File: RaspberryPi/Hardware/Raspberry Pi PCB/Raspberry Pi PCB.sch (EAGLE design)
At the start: 32 parts, among them Q11 BSS138, Q12 BSS138, Q2 BSS138

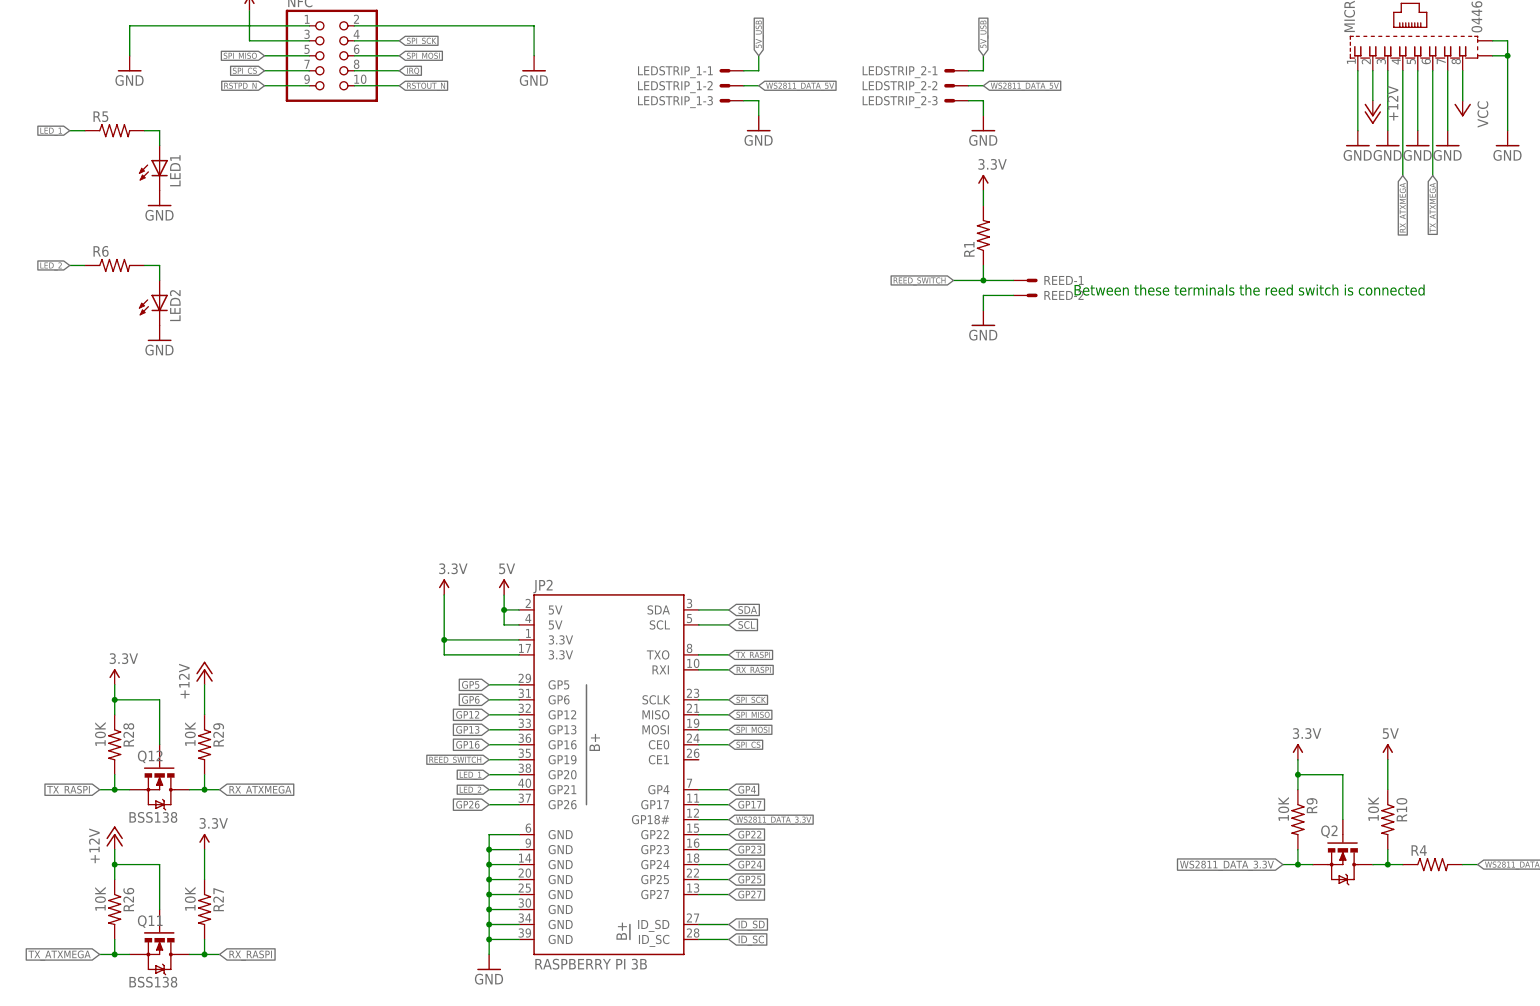
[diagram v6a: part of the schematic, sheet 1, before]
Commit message: Finished the first version of the Raspberry PCB.
Design rule check worked out fine. The PCB should now be ready for ordering.
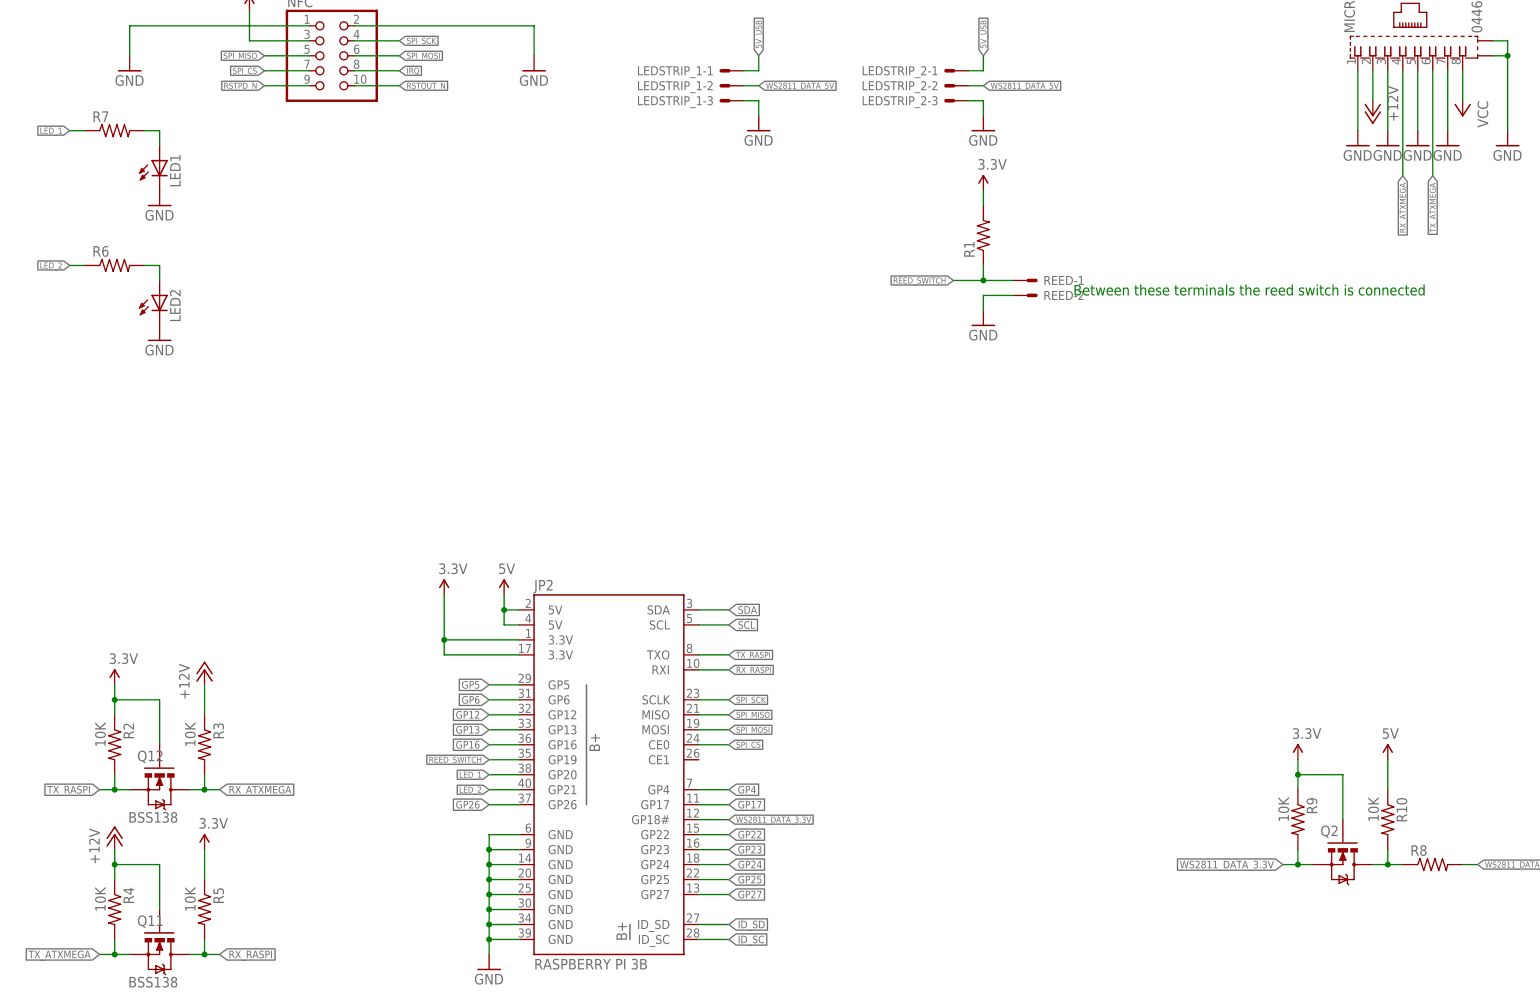
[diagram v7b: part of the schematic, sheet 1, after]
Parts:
- removed R26, R27: 10K, SparkFun:RESISTOR0603-RES
- added R7, R8: (no value), adafruit:R-US_R0805
- R4, R5: value (none) -> 10K; device adafruit:R-US_R0805 -> SparkFun:RESISTOR0603-RES
- renumbered C11 to C8, R28 to R2, R29 to R3
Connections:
- net +12V: now also R4.1; no longer R26.1
- net 3.3V: now also R5.1; no longer R27.1
- net LED_1: now also R7.1; no longer R5.1
- net N$3: now also R8.1; no longer R4.1
- net N$5: now also R7.2; no longer R5.2
- net RX_RASPI: now also R5.2; no longer R27.2
- net TX_ATXMEGA: now also R4.2; no longer R26.2
- net WS2811_DATA_5V: now also R8.2; no longer R4.2
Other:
- moved on the sheet: R4, R5
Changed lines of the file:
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@@
 <part name="SUPPLY14" library="SparkFun-Aesthetics" deviceset="3.3V" device=""/>
 <part name="Q11" library="SparkFun" deviceset="MOSFET-NCHANNEL" device="SMD" value="BSS138"/>
-<part name="R26" library="SparkFun" deviceset="RESISTOR" device="0603-RES" value="10K"/>
-<part name="R27" library="SparkFun" deviceset="RESISTOR" device="0603-RES" value="10K"/>
+<part name="R4" library="SparkFun" deviceset="RESISTOR" device="0603-RES" value="10K"/>
+<part name="R5" library="SparkFun" deviceset="RESISTOR" device="0603-RES" value="10K"/>
 <part name="Q12" library="SparkFun" deviceset="MOSFET-NCHANNEL" device="SMD" value="BSS138"/>
-<part name="R28" library="SparkFun" deviceset="RESISTOR" device="0603-RES" value="10K"/>
-<part name="R29" library="SparkFun" deviceset="RESISTOR" device="0603-RES" value="10K"/>
+<part name="R2" library="SparkFun" deviceset="RESISTOR" device="0603-RES" value="10K"/>
+<part name="R3" library="SparkFun" deviceset="RESISTOR" device="0603-RES" value="10K"/>
 <part name="P+51" library="supply1" library_urn="urn:adsk.eagle:library:371" deviceset="+12V" device=""/>
 <part name="P+52" library="supply1" library_urn="urn:adsk.eagle:library:371" deviceset="+12V" device=""/>
@@
 <part name="GND21" library="SparkFun" deviceset="GND" device=""/>
 <part name="GND22" library="SparkFun" deviceset="GND" device=""/>
-<part name="R4" library="adafruit" library_urn="urn:adsk.eagle:library:420" deviceset="R-US_" device="R0805"/>
-<part name="R5" library="adafruit" deviceset="R-US_" device="R0805"/>
+<part name="R8" library="adafruit" library_urn="urn:adsk.eagle:library:420" deviceset="R-US_" device="R0805"/>
+<part name="R7" library="adafruit" deviceset="R-US_" device="R0805"/>
 <part name="R6" library="adafruit" deviceset="R-US_" device="R0805"/>
 <part name="GND23" library="SparkFun" deviceset="GND" device=""/>
@@
 <part name="SUPPLY9" library="SparkFun-Aesthetics" deviceset="5V" device=""/>
 <part name="SUPPLY8" library="SparkFun-Aesthetics" deviceset="5V" device=""/>
-<part name="C11" library="SparkFun-Capacitors" library_urn="urn:adsk.eagle:library:510" deviceset="1.0UF" device="-0805-25V-(+80/-20%)" package3d_urn="urn:adsk.eagle:package:37429/1" value="100nF"/>
+<part name="C8" library="SparkFun-Capacitors" library_urn="urn:adsk.eagle:library:510" deviceset="1.0UF" device="-0805-25V-(+80/-20%)" package3d_urn="urn:adsk.eagle:package:37429/1" value="100nF"/>
 <part name="GND25" library="supply1" library_urn="urn:adsk.eagle:library:371" deviceset="GND" device=""/>
 <part name="USB_POWER" library="87520-0010BLF" deviceset="87520-0010BLF" device=""/>
@@
 <attribute name="VALUE" x="22.606" y="4.572" size="1.778" layer="96"/>
 </instance>
-<instance part="R26" gate="G$1" x="20.32" y="17.78" rot="R270"/>
-<instance part="R27" gate="G$1" x="35.56" y="17.78" rot="R270"/>
+<instance part="R4" gate="G$1" x="20.32" y="17.78" rot="R270"/>
+<instance part="R5" gate="G$1" x="35.56" y="17.78" rot="R270"/>
 <instance part="Q12" gate="G$1" x="27.94" y="38.1" smashed="yes" rot="R270">
 <attribute name="NAME" x="24.13" y="42.926" size="1.778" layer="95"/>
 <attribute name="VALUE" x="22.606" y="32.512" size="1.778" layer="96"/>
 </instance>
-<instance part="R28" gate="G$1" x="20.32" y="45.72" rot="R270"/>
-<instance part="R29" gate="G$1" x="35.56" y="45.72" rot="R270"/>
+<instance part="R2" gate="G$1" x="20.32" y="45.72" rot="R270"/>
+<instance part="R3" gate="G$1" x="35.56" y="45.72" rot="R270"/>
 <instance part="P+51" gate="1" x="35.56" y="58.42"/>
 <instance part="P+52" gate="1" x="20.32" y="30.48"/>
@@
 <instance part="GND21" gate="1" x="167.64" y="149.86"/>
 <instance part="GND22" gate="1" x="129.54" y="149.86"/>
-<instance part="R4" gate="G$1" x="243.84" y="25.4"/>
-<instance part="R5" gate="G$1" x="20.32" y="149.86"/>
+<instance part="R8" gate="G$1" x="243.84" y="25.4"/>
+<instance part="R7" gate="G$1" x="20.32" y="149.86"/>
 <instance part="R6" gate="G$1" x="20.32" y="127"/>
 <instance part="GND23" gate="1" x="27.94" y="137.16"/>
@@
 <wire x1="27.94" y1="53.34" x2="20.32" y2="53.34" width="0.1524" layer="91"/>
 <junction x="20.32" y="53.34"/>
-<pinref part="R28" gate="G$1" pin="1"/>
+<pinref part="R2" gate="G$1" pin="1"/>
 <pinref part="Q12" gate="G$1" pin="G"/>
 <pinref part="SUPPLY1" gate="G$1" pin="3.3V"/>
@@
 <segment>
 <wire x1="35.56" y1="22.86" x2="35.56" y2="27.94" width="0.1524" layer="91"/>
-<pinref part="R27" gate="G$1" pin="1"/>
+<pinref part="R5" gate="G$1" pin="1"/>
 <pinref part="SUPPLY2" gate="G$1" pin="3.3V"/>
 </segment>
@@
 </segment>
 <segment>
-<pinref part="R5" gate="G$1" pin="1"/>
+<pinref part="R7" gate="G$1" pin="1"/>
 <wire x1="15.24" y1="149.86" x2="12.7" y2="149.86" width="0.1524" layer="91"/>
 <label x="12.7" y="149.86" size="1.016" layer="95" rot="R180" xref="yes"/>
@@
 <junction x="20.32" y="38.1"/>
 <pinref part="Q12" gate="G$1" pin="S"/>
-<pinref part="R28" gate="G$1" pin="2"/>
+<pinref part="R2" gate="G$1" pin="2"/>
 <label x="17.78" y="38.1" size="1.27" layer="95" rot="R180" xref="yes"/>
 </segment>
@@
 <segment>
 <wire x1="35.56" y1="50.8" x2="35.56" y2="55.88" width="0.1524" layer="91"/>
-<pinref part="R29" gate="G$1" pin="1"/>
+<pinref part="R3" gate="G$1" pin="1"/>
 <pinref part="P+51" gate="1" pin="+12V"/>
 </segment>
@@
 <wire x1="27.94" y1="25.4" x2="20.32" y2="25.4" width="0.1524" layer="91"/>
 <junction x="20.32" y="25.4"/>
-<pinref part="R26" gate="G$1" pin="1"/>
+<pinref part="R4" gate="G$1" pin="1"/>
 <pinref part="Q11" gate="G$1" pin="G"/>
 <pinref part="P+52" gate="1" pin="+12V"/>
@@
 <junction x="35.56" y="38.1"/>
 <pinref part="Q12" gate="G$1" pin="D"/>
-<pinref part="R29" gate="G$1" pin="2"/>
+<pinref part="R3" gate="G$1" pin="2"/>
 <label x="38.1" y="38.1" size="1.27" layer="95" xref="yes"/>
 </segment>
@@
 <junction x="20.32" y="10.16"/>
 <pinref part="Q11" gate="G$1" pin="S"/>
-<pinref part="R26" gate="G$1" pin="2"/>
+<pinref part="R4" gate="G$1" pin="2"/>
 <label x="17.78" y="10.16" size="1.27" layer="95" rot="R180" xref="yes"/>
 </segment>
@@
 <junction x="35.56" y="10.16"/>
 <pinref part="Q11" gate="G$1" pin="D"/>
-<pinref part="R27" gate="G$1" pin="2"/>
+<pinref part="R5" gate="G$1" pin="2"/>
 <label x="38.1" y="10.16" size="1.27" layer="95" xref="yes"/>
 </segment>
@@
 <segment>
 <pinref part="LED1" gate="G$1" pin="A"/>
-<pinref part="R5" gate="G$1" pin="2"/>
+<pinref part="R7" gate="G$1" pin="2"/>
 <wire x1="27.94" y1="147.32" x2="27.94" y2="149.86" width="0.1524" layer="91"/>
 <wire x1="27.94" y1="149.86" x2="25.4" y2="149.86" width="0.1524" layer="91"/>
@@
 </segment>
 <segment>
-<pinref part="R4" gate="G$1" pin="2"/>
+<pinref part="R8" gate="G$1" pin="2"/>
 <wire x1="248.92" y1="25.4" x2="251.46" y2="25.4" width="0.1524" layer="91"/>
 <label x="251.46" y="25.4" size="1.016" layer="95" xref="yes"/>
@@
 <net name="N$3" class="0">
 <segment>
-<pinref part="R4" gate="G$1" pin="1"/>
+<pinref part="R8" gate="G$1" pin="1"/>
 <pinref part="Q2" gate="G$1" pin="D"/>
 <wire x1="238.76" y1="25.4" x2="236.22" y2="25.4" width="0.1524" layer="91"/>
@@
 <instance part="GND10" gate="1" x="45.72" y="116.84"/>
 <instance part="SUPPLY8" gate="G$1" x="45.72" y="134.62"/>
-<instance part="C11" gate="G$1" x="-10.16" y="124.46"/>
+<instance part="C8" gate="G$1" x="-10.16" y="124.46"/>
 <instance part="GND25" gate="1" x="-10.16" y="116.84"/>
 <instance part="USB_POWER" gate="G$1" x="172.72" y="124.46"/>
@@
 <segment>
 <pinref part="GND25" gate="1" pin="GND"/>
-<pinref part="C11" gate="G$1" pin="2"/>
+<pinref part="C8" gate="G$1" pin="2"/>
 <wire x1="-10.16" y1="119.38" x2="-10.16" y2="121.92" width="0.1524" layer="91"/>
 </segment>
@@
 <junction x="-20.32" y="132.08"/>
 <label x="-2.54" y="132.08" size="1.016" layer="95" xref="yes"/>
-<pinref part="C11" gate="G$1" pin="1"/>
+<pinref part="C8" gate="G$1" pin="1"/>
 <wire x1="-10.16" y1="132.08" x2="-2.54" y2="132.08" width="0.1524" layer="91"/>
 <wire x1="-10.16" y1="129.54" x2="-10.16" y2="132.08" width="0.1524" layer="91"/>

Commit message: The Raspberry PCB is almost finished now.
The buttons and the jumper has been included. The size has been increased. All the primary functionality has been finished now.
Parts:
- added BUTTON1, BUTTON2, BUTTON3, BUTTON4, BUTTON5, BUTTON6, BUTTON7, BUTTON8: 22-05-7028-02, con-molex:22-05-7028-02
- added C10, C9: 100nF, SparkFun-Capacitors:1.0UF-0805-25V-(+80/-20%)
- added JUMPER: (no value), jumper:JP2E
- added R11, R12, R13, R14, R15, R16, R17, R18, R19, R20, R21, R22, R23, R24, R25, R26: 10K, SparkFun:RESISTOR0603-RES
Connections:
- removed net GP12: JP2.GP12
- removed net GP13: JP2.GP13
- removed net GP16: JP2.GP16
- removed net GP22: JP2.GP22
- removed net GP26: JP2.GP26
- removed net GP27: JP2.GP27
- removed net GP5: JP2.GP5
- removed net GP6: JP2.GP6
- new net BUTTON1: JP2.GP20, R12.2
- new net BUTTON2: JP2.GP21, R14.2
- new net BUTTON3: JP2.GP26, R16.2
- new net BUTTON4: JP2.GP16, R18.2
- new net BUTTON5: JP2.GP19, R20.2
- new net BUTTON6: JP2.GP13, R22.2
- new net BUTTON7: JP2.GP12, R24.2
- new net BUTTON8: JP2.GP6, R26.2
- new net N$1: C10.1, JUMPER.3, REED-1.S
- new net N$10: BUTTON6-1.S, R21.2, R22.1
- new net N$11: BUTTON7-1.S, R23.2, R24.1
- new net N$12: BUTTON8-1.S, R25.2, R26.1
- new net N$2: BUTTON2-1.S, R13.2, R14.1
- new net N$6: BUTTON1-1.S, R11.2, R12.1
- new net N$7: BUTTON3-1.S, R15.2, R16.1
- new net N$8: BUTTON4-1.S, R17.2, R18.1
- new net N$9: BUTTON5-1.S, R19.2, R20.1
- net 3.3V: now also R11.1, R13.1, R15.1, R17.1, R19.1, R21.1, R23.1, R25.1
- net 5V_USB: now also C9.1
- net GND: now also BUTTON1-2.S, BUTTON2-2.S, BUTTON3-2.S, BUTTON4-2.S, BUTTON5-2.S, BUTTON6-2.S, BUTTON7-2.S, BUTTON8-2.S, C10.2, C9.2, JUMPER.1
- net LED_1: now also JP2.GP27; no longer JP2.GP20
- net LED_2: now also JP2.GP22; no longer JP2.GP21
- net REED_SWITCH: now also JP2.GP5, JUMPER.2; no longer JP2.GP19, REED-1.S
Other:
- note added: "When the door is open this pin is HIGH"
- note added: "kolommen selectie: 4 of 8 stuks"
- moved on the sheet: NFC, R1, REED-1, REED-2
